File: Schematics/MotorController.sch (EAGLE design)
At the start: 47 parts, among them IC1 MEGA164P/324P/644P-AU, IC3 LM324N

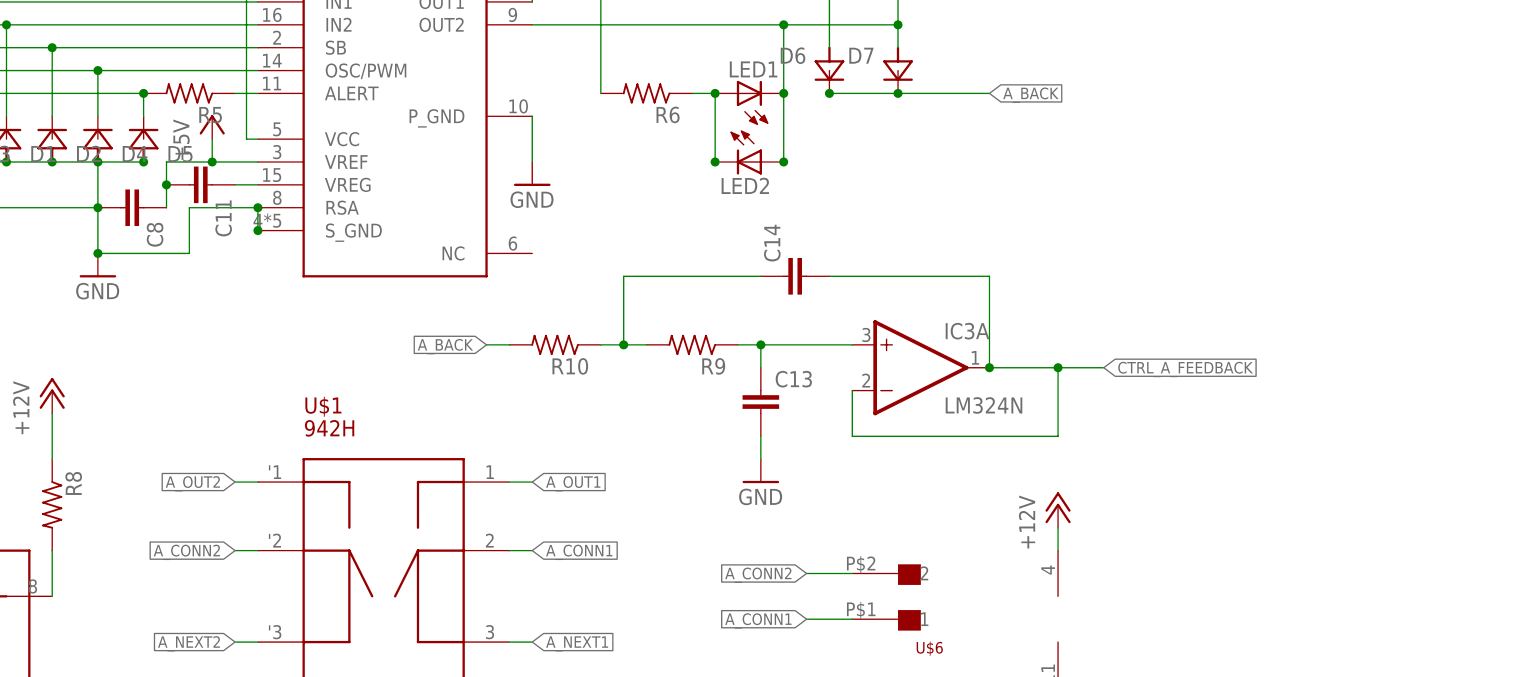
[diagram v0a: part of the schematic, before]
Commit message: add files of device software newly created
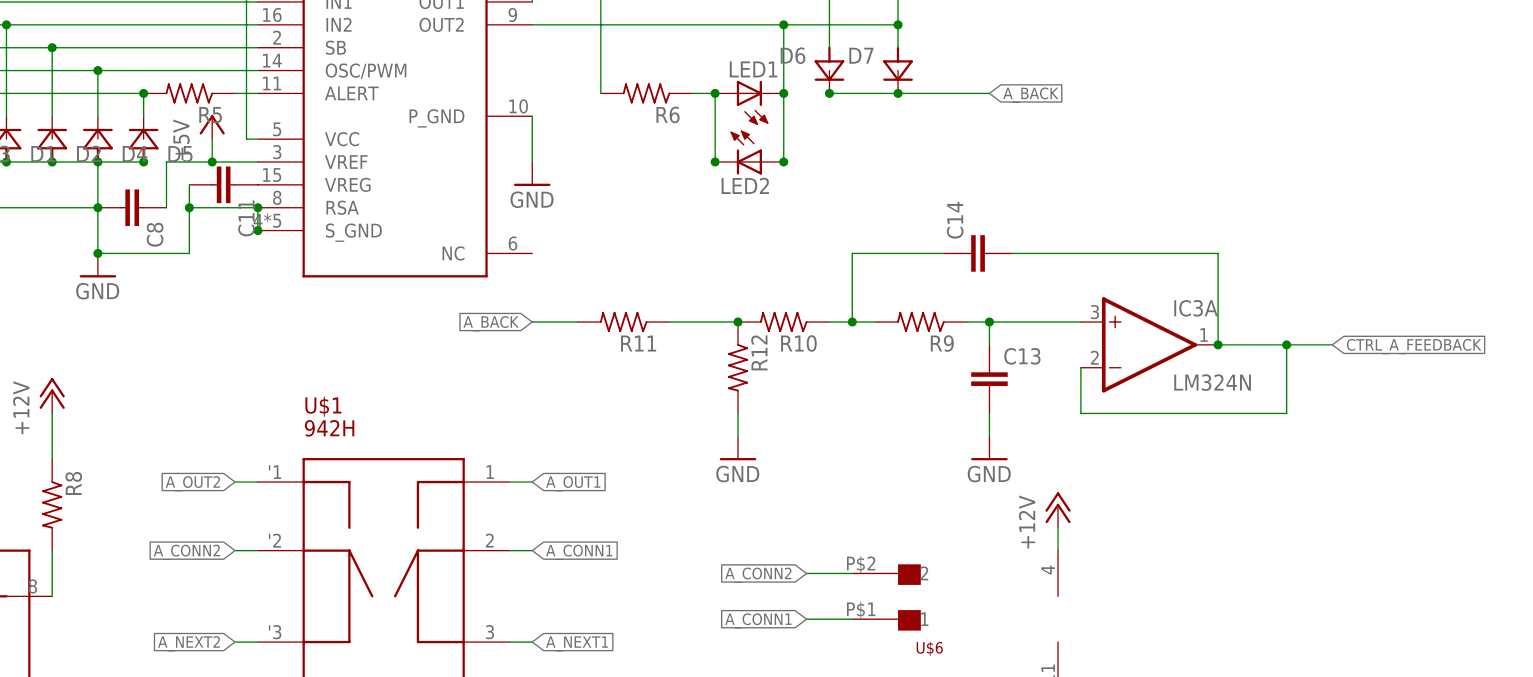
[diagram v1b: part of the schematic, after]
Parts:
- added R11, R12: (no value), rcl:R-US_M3216
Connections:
- new net N$14: R10.2, R11.1, R12.1
- net +5V: no longer C11.2
- net A_BACK: now also R11.2; no longer R10.2
- net GND: now also C11.2, R12.2
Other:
- moved on the sheet: C11, C13, C14, IC3A, R10, R9
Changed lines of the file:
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@@
 <part name="P+9" library="supply1" deviceset="+12V" device=""/>
 <part name="GND11" library="supply1" deviceset="GND" device=""/>
+<part name="R11" library="rcl" deviceset="R-US_" device="M3216"/>
+<part name="R12" library="rcl" deviceset="R-US_" device="M3216"/>
+<part name="GND12" library="supply1" deviceset="GND" device=""/>
 </parts>
 <sheets>
@@
 <instance part="C10" gate="G$1" x="226.06" y="154.94"/>
 <instance part="GND6" gate="1" x="226.06" y="142.24"/>
-<instance part="C11" gate="G$1" x="177.8" y="116.84" rot="R270"/>
+<instance part="C11" gate="G$1" x="180.34" y="116.84" rot="R270"/>
 <instance part="U$4" gate="G$1" x="185.42" y="157.48"/>
 <instance part="R4" gate="G$1" x="142.24" y="119.38" rot="R90"/>
@@
 <instance part="C12" gate="G$1" x="119.38" y="124.46"/>
 <instance part="GND7" gate="1" x="213.36" y="116.84"/>
-<instance part="IC3" gate="A" x="256.54" y="96.52"/>
+<instance part="IC3" gate="A" x="281.94" y="99.06"/>
 <instance part="LED1" gate="G$1" x="236.22" y="127" rot="R90"/>
 <instance part="LED2" gate="G$1" x="238.76" y="119.38" rot="R270"/>
@@
 <instance part="U$6" gate="G$1" x="254" y="76.2" rot="R180"/>
 <instance part="U$7" gate="G$1" x="254" y="58.42" rot="R180"/>
-<instance part="R9" gate="G$1" x="231.14" y="99.06" rot="R180"/>
-<instance part="R10" gate="G$1" x="215.9" y="99.06" rot="R180"/>
-<instance part="C13" gate="G$1" x="238.76" y="93.98"/>
-<instance part="C14" gate="G$1" x="241.3" y="106.68" rot="R90"/>
-<instance part="GND10" gate="1" x="238.76" y="83.82"/>
+<instance part="R9" gate="G$1" x="256.54" y="101.6" rot="R180"/>
+<instance part="R10" gate="G$1" x="241.3" y="101.6" rot="R180"/>
+<instance part="C13" gate="G$1" x="264.16" y="96.52"/>
+<instance part="C14" gate="G$1" x="261.62" y="109.22" rot="R90"/>
+<instance part="GND10" gate="1" x="264.16" y="86.36"/>
 <instance part="L2" gate="G$1" x="12.7" y="83.82" rot="R90"/>
 <instance part="IC3" gate="P" x="271.78" y="68.58"/>
 <instance part="P+9" gate="1" x="271.78" y="81.28"/>
 <instance part="GND11" gate="1" x="271.78" y="55.88"/>
+<instance part="R11" gate="G$1" x="223.52" y="101.6" rot="R180"/>
+<instance part="R12" gate="G$1" x="236.22" y="96.52" rot="R270"/>
+<instance part="GND12" gate="1" x="236.22" y="86.36"/>
 </instances>
 <busses>
@@
 </segment>
 <segment>
-<pinref part="C8" gate="G$1" pin="1"/>
-<wire x1="172.72" y1="114.3" x2="172.72" y2="116.84" width="0.1524" layer="91"/>
-<wire x1="172.72" y1="116.84" x2="172.72" y2="119.38" width="0.1524" layer="91"/>
 <wire x1="182.88" y1="119.38" x2="177.8" y2="119.38" width="0.1524" layer="91"/>
 <pinref part="P+3" gate="1" pin="+5V"/>
@@
 <wire x1="177.8" y1="121.92" x2="177.8" y2="119.38" width="0.1524" layer="91"/>
 <junction x="177.8" y="119.38"/>
-<pinref part="C11" gate="G$1" pin="2"/>
-<junction x="172.72" y="116.84"/>
 <pinref part="U$3" gate="G$1" pin="VREF"/>
+<pinref part="C8" gate="G$1" pin="1"/>
+<wire x1="172.72" y1="119.38" x2="172.72" y2="114.3" width="0.1524" layer="91"/>
 </segment>
 </net>
@@
 <junction x="170.18" y="119.38"/>
 <junction x="182.88" y="114.3"/>
+<pinref part="C11" gate="G$1" pin="2"/>
+<wire x1="175.26" y1="116.84" x2="175.26" y2="114.3" width="0.1524" layer="91"/>
+<junction x="175.26" y="114.3"/>
 </segment>
 <segment>
@@
 <pinref part="C13" gate="G$1" pin="2"/>
 <pinref part="GND10" gate="1" pin="GND"/>
-<wire x1="238.76" y1="88.9" x2="238.76" y2="86.36" width="0.1524" layer="91"/>
+<wire x1="264.16" y1="91.44" x2="264.16" y2="88.9" width="0.1524" layer="91"/>
 </segment>
 <segment>
@@
 <pinref part="GND11" gate="1" pin="GND"/>
 <wire x1="271.78" y1="58.42" x2="271.78" y2="60.96" width="0.1524" layer="91"/>
+</segment>
+<segment>
+<pinref part="R12" gate="G$1" pin="2"/>
+<pinref part="GND12" gate="1" pin="GND"/>
+<wire x1="236.22" y1="91.44" x2="236.22" y2="88.9" width="0.1524" layer="91"/>
 </segment>
 </net>
@@
 <segment>
 <pinref part="C11" gate="G$1" pin="1"/>
-<wire x1="180.34" y1="116.84" x2="182.88" y2="116.84" width="0.1524" layer="91"/>
 <pinref part="U$3" gate="G$1" pin="VREG"/>
 </segment>
@@
 <segment>
 <pinref part="C14" gate="G$1" pin="2"/>
-<wire x1="246.38" y1="106.68" x2="264.16" y2="106.68" width="0.1524" layer="91"/>
+<wire x1="266.7" y1="109.22" x2="289.56" y2="109.22" width="0.1524" layer="91"/>
 <pinref part="IC3" gate="A" pin="OUT"/>
-<wire x1="264.16" y1="106.68" x2="264.16" y2="96.52" width="0.1524" layer="91"/>
-<wire x1="264.16" y1="96.52" x2="271.78" y2="96.52" width="0.1524" layer="91"/>
+<wire x1="289.56" y1="109.22" x2="289.56" y2="99.06" width="0.1524" layer="91"/>
+<wire x1="289.56" y1="99.06" x2="297.18" y2="99.06" width="0.1524" layer="91"/>
 <pinref part="IC3" gate="A" pin="-IN"/>
-<wire x1="248.92" y1="93.98" x2="248.92" y2="88.9" width="0.1524" layer="91"/>
-<wire x1="248.92" y1="88.9" x2="271.78" y2="88.9" width="0.1524" layer="91"/>
-<wire x1="271.78" y1="88.9" x2="271.78" y2="96.52" width="0.1524" layer="91"/>
-<wire x1="271.78" y1="96.52" x2="276.86" y2="96.52" width="0.1524" layer="91"/>
-<junction x="264.16" y="96.52"/>
-<junction x="271.78" y="96.52"/>
-<label x="276.86" y="96.52" size="1.27" layer="95" xref="yes"/>
+<wire x1="274.32" y1="96.52" x2="274.32" y2="91.44" width="0.1524" layer="91"/>
+<wire x1="274.32" y1="91.44" x2="297.18" y2="91.44" width="0.1524" layer="91"/>
+<wire x1="297.18" y1="91.44" x2="297.18" y2="99.06" width="0.1524" layer="91"/>
+<wire x1="297.18" y1="99.06" x2="302.26" y2="99.06" width="0.1524" layer="91"/>
+<junction x="289.56" y="99.06"/>
+<junction x="297.18" y="99.06"/>
+<label x="302.26" y="99.06" size="1.27" layer="95" xref="yes"/>
 </segment>
 </net>
@@
 </segment>
 <segment>
-<pinref part="R10" gate="G$1" pin="2"/>
-<wire x1="210.82" y1="99.06" x2="208.28" y2="99.06" width="0.1524" layer="91"/>
-<label x="208.28" y="99.06" size="1.27" layer="95" rot="R180" xref="yes"/>
+<pinref part="R11" gate="G$1" pin="2"/>
+<wire x1="218.44" y1="101.6" x2="213.36" y2="101.6" width="0.1524" layer="91"/>
+<label x="213.36" y="101.6" size="1.27" layer="95" rot="R180" xref="yes"/>
 </segment>
 </net>
@@
 <pinref part="R10" gate="G$1" pin="1"/>
 <pinref part="R9" gate="G$1" pin="2"/>
-<wire x1="220.98" y1="99.06" x2="223.52" y2="99.06" width="0.1524" layer="91"/>
-<wire x1="223.52" y1="99.06" x2="226.06" y2="99.06" width="0.1524" layer="91"/>
-<wire x1="223.52" y1="99.06" x2="223.52" y2="106.68" width="0.1524" layer="91"/>
+<wire x1="246.38" y1="101.6" x2="248.92" y2="101.6" width="0.1524" layer="91"/>
+<wire x1="248.92" y1="101.6" x2="251.46" y2="101.6" width="0.1524" layer="91"/>
+<wire x1="248.92" y1="101.6" x2="248.92" y2="109.22" width="0.1524" layer="91"/>
 <pinref part="C14" gate="G$1" pin="1"/>
-<wire x1="223.52" y1="106.68" x2="238.76" y2="106.68" width="0.1524" layer="91"/>
-<junction x="223.52" y="99.06"/>
+<wire x1="248.92" y1="109.22" x2="259.08" y2="109.22" width="0.1524" layer="91"/>
+<junction x="248.92" y="101.6"/>
 </segment>
 </net>
@@
 <pinref part="R9" gate="G$1" pin="1"/>
 <pinref part="IC3" gate="A" pin="+IN"/>
-<wire x1="236.22" y1="99.06" x2="238.76" y2="99.06" width="0.1524" layer="91"/>
+<wire x1="261.62" y1="101.6" x2="264.16" y2="101.6" width="0.1524" layer="91"/>
 <pinref part="C13" gate="G$1" pin="1"/>
-<wire x1="238.76" y1="99.06" x2="248.92" y2="99.06" width="0.1524" layer="91"/>
-<wire x1="238.76" y1="99.06" x2="238.76" y2="96.52" width="0.1524" layer="91"/>
-<junction x="238.76" y="99.06"/>
+<wire x1="264.16" y1="101.6" x2="274.32" y2="101.6" width="0.1524" layer="91"/>
+<wire x1="264.16" y1="101.6" x2="264.16" y2="99.06" width="0.1524" layer="91"/>
+<junction x="264.16" y="101.6"/>
 </segment>
 </net>
@@
 </segment>
 </net>
+<net name="N$14" class="0">
+<segment>
+<pinref part="R10" gate="G$1" pin="2"/>
+<pinref part="R12" gate="G$1" pin="1"/>
+<pinref part="R11" gate="G$1" pin="1"/>
+<wire x1="236.22" y1="101.6" x2="228.6" y2="101.6" width="0.1524" layer="91"/>
+<junction x="236.22" y="101.6"/>
+</segment>
+</net>

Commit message: restoring
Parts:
- removed D5, D6, D7, D8: 1SS196, myparts:1SS196
- removed L2: (no value), rcl:L-USL3216C
- removed U$5: TLP621-2, myparts:TLP621-2
- removed U$6, U$7: XH-2, myparts:XH-2
- added A, B, C, D: 942H, myparts:942H
- added A_NEXT, A_PREV, B_NEXT, B_PREV, C_NEXT, C_PREV, D_NEXT, D_PREV: XH-2, myparts:XH-2
- added C15, C18, C19, C24, C25: 0.1u, rcl:C-EUC0603
- added C16, C17: 0.47u, rcl:C-EUC0603
- added C20, C21: 22p, rcl:C-EUC0603
- added C22, C23: 4.7u, rcl:C-EUC0603
- added C26, C27: (no value), rcl:CPOL-EUE2,5-6E
- added CONN: TUS_MODULE_SUPPLY, tus:TUS_MODULE_SUPPLY
- added F1, F2, F3, F4, F5: POLYSWITCH_20204/5, myparts:POLYSWITCH_20204/5
- added IC2: MEGA164P/324P/644P-AU, avr-7:MEGA164P/324P/644P-AU
- added IC4: TLP621-2, myparts:TLP621-2
- added LED3, LED5, LED7: G, led:LED3MM
- added LED4, LED6, LED8: O, led:LED3MM
- added R13, R14, R23, R24: 100, resistor:R-EU_R0603
- added R15, R16, R22, R25: 25k, resistor:R-EU_R0603
- added R17, R18, R20, R21, R30, R31: 3.3k, resistor:R-EU_R0603
- added R19, R36, R37: 10k, resistor:R-EU_R0603
- added R26, R27: 0.01, resistor:R-EU_R1206
- added R28, R29: 33k, resistor:R-EU_R0603
- added R32, R33: 500, resistor:R-EU_R0603
- added R34, R35: 100k, resistor:R-EU_R0603
- added T1, T2, T3, T4: 2SC1815, myparts:2SC1815
- C1, C2: device rcl:C-EUC1608 -> rcl:CPOL-EUE2,5-6E
- C10: value (none) -> 0.47u; device rcl:CPOL-EUE2-5 -> rcl:C-EUC0603
- C11, C7, C8: value (none) -> 0.1u; device rcl:C-EUC1608 -> rcl:C-EUC0603
- C12: value (none) -> 100u; device rcl:C-EUC1608 -> rcl:CPOL-EUE2.5-6
- C13: value (none) -> 0.1u; device rcl:C-EUC3216 -> rcl:C-EUC0603
- C14: value (none) -> 100u; device rcl:C-EUC3216 -> rcl:CPOL-EUE2-5
- C3: value (none) -> 0.1u; device rcl:CPOL-EUE2-5 -> rcl:C-EUC0603
- C4: value (none) -> 0.1u; device rcl:CPOL-EUE2.5-6 -> rcl:C-EUC0603
- C5, C6: value (none) -> 4.7u; device rcl:C-EUC1608 -> rcl:C-EUC0603
- C9: value (none) -> 0.47u; device rcl:C-EUC1608 -> rcl:C-EUC0603
- D1, D2, D3, D4: value 1SS196 -> 1N4148DO35-7; device myparts:1SS196 -> diode:1N4148DO35-7
- IC1: value MEGA164P/324P/644P-AU -> TLP621-2; device avr-7:MEGA164P/324P/644P-AU -> myparts:TLP621-2
- IC3: value LM324N -> OPA4234P; device linear:LM324N -> burr-brown:OPA4234P
- JP1: value AVR-JTAG-10-R -> AVR-JTAG-10; device avr-7:AVR-JTAG-10-R -> avr-7:AVR-JTAG-10
- L1: value (none) -> 47u; device rcl:L-USL3216C -> rcl:L-EUL3216C
- LED1: value (none) -> G
- LED2: value (none) -> O
- Q1: value (none) -> 20.000M
- R1, R6: value (none) -> 100k; device rcl:R-US_M3216 -> resistor:R-EU_R0603
- R10, R9: value (none) -> 33k; device rcl:R-US_M3216 -> resistor:R-EU_R0603
- R11, R12: value (none) -> 0.01; device rcl:R-US_M3216 -> resistor:R-EU_R1206
- R2, R4: value 100k -> 10k; device rcl:R-US_M3216 -> resistor:R-EU_R0603
- R3: value 100k -> 500; device rcl:R-US_M3216 -> resistor:R-EU_R0603
- R5: value (none) -> 500; device rcl:R-US_M3216 -> resistor:R-EU_R0603
- R7, R8: value (none) -> 3.3k; device rcl:R-US_M3216 -> resistor:R-EU_R0603
- U$1: value 942H -> TB6559; device myparts:942H -> myparts:TB6559
- U$2: value TUS_MODULE_SUPPLY -> TB6559; device tus:TUS_MODULE_SUPPLY -> myparts:TB6559
- U$4: value POLYSWITCH_20207/10 -> TB6559; device myparts:POLYSWITCH_20207/10 -> myparts:TB6559
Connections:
- removed net A_BACK: D6.A, D7.A, R11.2
- removed net A_CONN1: U$1.2, U$6.1
- removed net A_CONN2: U$1.'2, U$6.2
- removed net A_NEXT1: U$1.3, U$7.1
- removed net A_NEXT2: U$1.'3, U$7.2
- removed net CTRL_A_FEEDBACK: C14.2, IC1.(ADC0/PCINT0)PA0, IC3A.-IN, IC3A.OUT
- removed net CTRL_B_FEEDBACK: IC1.(ADC1/PCINT1)PA1
- removed net CTRL_C_FEEDBACK: IC1.(ADC2/PCINT2)PA2
- removed net CTRL_D_FEEDBACK: IC1.(ADC3/PCINT3)PA3
- removed net CTRL_PWM: D4.A, U$3.OSC/PWM
- new net A_OUT3: C.1, R20.2, U$3.OUT1
- new net A_OUT4: C.'1, LED5.A, LED6.C, U$3.OUT2
- new net A_OUT5: B.1, R18.2, U$2.OUT1
- new net A_OUT6: B.'1, LED1.A, LED2.C, U$2.OUT2
- new net A_OUT7: D.1, R21.2, U$4.OUT1
- new net A_OUT8: D.'1, LED7.A, LED8.C, U$4.OUT2
- new net D: D.3, D_PREV.2
- new net FEEDBACK_A: IC2.(ADC2/PCINT2)PA2, IC3A.OUT, R16.2
- new net FEEDBACK_B: IC2.(ADC3/PCINT3)PA3, IC3B.OUT, R15.2
- new net FEEDBACK_C: IC2.(ADC1/PCINT1)PA1, IC3D.OUT, R25.2
- new net FEEDBACK_D: IC2.(ADC0/PCINT0)PA0, IC3C.OUT, R22.2
- new net N$15: A.'2, A_NEXT.1
- new net N$16: A.3, A_PREV.2
- new net N$17: A.'3, A_PREV.1
- new net N$18: C18.2, C27.+, F4.1, U$3.VCC
- new net N$19: LED5.C, LED6.A, R20.1
- new net N$20: IC1G$2.1, R5.2
- new net N$21: C9.1, IC3A.+IN, R9.2
- new net N$22: C.2, C_NEXT.2
- new net N$23: C.'2, C_NEXT.1
- new net N$24: C.3, C_PREV.2
- new net N$25: C.'3, C_PREV.1
- new net N$26: IC4G$2.4, R35.1, R36.1
- new net N$27: C.'4, D3.C, T3.E
- new net N$28: R36.2, T3.B
- new net N$29: IC3D.-IN, R24.1, R25.1
- new net N$30: C16.1, IC3D.+IN, R28.2
- new net N$31: R26.1, R28.1, U$3.P_GND
- new net N$32: C4.1, U$2.VREG
- new net N$33: R8.1, U$2.ALERT
- new net N$34: C2.+, C8.2, F1.1, U$2.VCC
- new net N$35: LED1.C, LED2.A, R18.1
- new net N$36: IC4G$1.1, R33.2
- new net N$37: B.2, B_NEXT.2
- new net N$38: B.'2, B_NEXT.1
- new net N$39: B.3, B_PREV.2
- new net N$40: B.'3, B_PREV.1
- new net N$41: IC1G$2.4, R1.1, R4.1
- new net N$42: B.'4, D2.C, T1.E
- new net N$43: R4.2, T1.B
- new net N$44: IC3B.-IN, R13.1, R15.1
- new net N$45: C10.1, IC3B.+IN, R10.2
- new net N$46: R10.1, R12.1, U$2.P_GND
- new net N$47: C25.1, U$4.VREG
- new net N$48: R31.1, U$4.ALERT
- new net N$49: C19.2, C26.+, F5.1, U$4.VCC
- new net N$50: LED7.C, LED8.A, R21.1
- new net N$51: IC4G$2.1, R32.2
- new net N$52: D.2, D_NEXT.2
- new net N$53: D.'2, D_NEXT.1
- new net N$54: CONN.6_5V, F3.1
- new net N$55: D.'3, D_PREV.1
- new net N$56: IC4G$1.4, R34.1, R37.1
- new net N$57: D.'4, D4.C, T4.E
- new net N$58: R37.2, T4.B
- new net N$59: IC3C.-IN, R22.1, R23.1
- new net N$60: C17.1, IC3C.+IN, R29.2
- new net N$61: R27.1, R29.1, U$4.P_GND
- new net N$84: A.'4, D1.C, T2.E
- new net N$86: R2.2, T2.B
- net !RESET: now also CONN.15_!RESET, IC2.!RESET, JP1.6, R19.2; no longer IC1.!RESET, R1.2, U$2.15_!RESET
- net !SS: now also CONN.11_!SS, IC2.(OC0B/!SS!/PCINT12)PB4; no longer IC1.(OC0B/!SS!/PCINT12)PB4, U$2.11_!SS
- net +12V: now also C12.+, CONN.1_12V, CONN.2_12V, CONN.4_12V, F1.2, F2.2, F4.2, F5.2, IC1G$1.3, IC1G$2.3, IC4G$1.3, IC4G$2.3, T1.C, T2.C, T3.C, T4.C; no longer C10.+, C4.+, C9.2, D8.A, IC3P.V+, R8.1, U$2.1_12V, U$2.2_12V, U$2.4_12V, U$4.2
- net +5V: now also C11.2, C13.2, C14.+, C15.2, F3.2, IC2.VCC@1, IC2.VCC@2, IC2.VCC@3, IC3A.V+, R19.1, U$1.VREF, U$2.VREF, U$4.VREF; no longer C3.+, C5.2, C6.2, C7.2, C8.1, IC1.VCC@1, IC1.VCC@2, IC1.VCC@3, L2.1, R1.1, U$2.6_5V
- net A_OUT1: now also A.1, R17.2, U$1.OUT1; no longer D6.C, R6.2, U$1.1, U$3.OUT1
- net A_OUT2: now also A.'1, LED3.A, LED4.C, U$1.OUT2; no longer D7.C, LED1.C, LED2.A, U$1.'1, U$3.OUT2
- net CTRL_A_1: now also IC2.(ADC5/PCINT5)PA5, U$1.IN1; no longer D3.A, IC1.(RXD0/PCINT24)PD0, R2.2, U$3.IN1
- net CTRL_A_2: now also IC2.(ADC6/PCINT6)PA6, U$1.IN2; no longer D1.A, IC1.(TXD0/PCINT25)PD1, R3.2, U$3.IN2
- net CTRL_A_3: now also IC2.(ADC4/PCINT4)PA4, R3.1, U$1.SB; no longer D2.A, IC1.(RXD1/INT0/PCINT26)PD2, R4.2, R7.1, U$3.SB
- net CTRL_A_ALERT: now also C5.1, IC2.(ADC7/PCINT7)PA7, R7.2; no longer C12.1, D5.A, IC1.(TXD1/INT1/PCINT27)PD3, R5.2
- net CTRL_A_PWM: now also IC2.(OC2B/ICP/PCINT30)PD6, U$1.OSC/PWM; no longer IC1.(OC1A/PCINT29)PD5
- net CTRL_B_1: now also IC2.(INT2/AIN0/PCINT10)PB2, U$2.IN1; no longer IC1.(SCL/PCINT16)PC0
- net CTRL_B_2: now also IC2.(CLKO/T1/PCINT9)PB1, U$2.IN2; no longer IC1.(SDA/PCINT17)PC1
- net CTRL_B_3: now also IC2.(OC0A/AIN1/PCINT11)PB3, R5.1, U$2.SB; no longer IC1.(TOSC1/PCINT22)PC6
- net CTRL_B_ALERT: now also C6.1, IC2.(XCK0/T0/PCINT8)PB0, R8.2; no longer IC1.(TOSC2/PCINT23)PC7
- net CTRL_B_PWM: now also IC2.(XCK1/OC1B/PCINT28)PD4, U$2.OSC/PWM; no longer IC1.(XCK1/OC1B/PCINT28)PD4
- net CTRL_C_1: now also IC2.(RXD1/INT0/PCINT26)PD2, U$3.IN1; no longer IC1.(XCK0/T0/PCINT8)PB0
- net CTRL_C_2: now also IC2.(TXD0/PCINT25)PD1, U$3.IN2; no longer IC1.(CLKO/T1/PCINT9)PB1
- net CTRL_C_3: now also IC2.(TXD1/INT1/PCINT27)PD3, R32.1, U$3.SB; no longer IC1.(INT2/AIN0/PCINT10)PB2
- net CTRL_C_ALERT: now also C22.1, IC2.(RXD0/PCINT24)PD0, R30.2; no longer IC1.(OC0A/AIN1/PCINT11)PB3
- net CTRL_C_PWM: now also IC2.(OC2A/PCINT31)PD7, U$3.OSC/PWM; no longer IC1.(OC2A/PCINT31)PD7
- net CTRL_D_1: now also IC2.(TOSC2/PCINT23)PC7, U$4.IN1; no longer IC1.(ADC4/PCINT4)PA4
- net CTRL_D_2: now also IC2.(TOSC1/PCINT22)PC6, U$4.IN2; no longer IC1.(ADC5/PCINT5)PA5
- net CTRL_D_3: now also IC2.(SCL/PCINT16)PC0, R33.1, U$4.SB; no longer IC1.(ADC6/PCINT6)PA6
- net CTRL_D_ALERT: now also C23.1, IC2.(SDA/PCINT17)PC1, R31.2; no longer IC1.(ADC7/PCINT7)PA7
- net CTRL_D_PWM: now also IC2.(OC1A/PCINT29)PD5, U$4.OSC/PWM; no longer IC1.(OC2B/ICP/PCINT30)PD6
- net GND: now also A.4, B.4, C.4, C1.-, C10.2, C11.1, C12.-, C13.1, C14.-, C15.1, C16.2, C17.2, C18.1, C19.1, C2.-, C20.1, C21.1, C22.2, C23.2, C24.2, C25.2, C26.-, C27.-, C3.2, C4.2, C5.2, C6.2, C8.1, C9.2, CONN.12_GND, CONN.3_GND, CONN.5_GND, CONN.7_GND, CONN.8_GND, CONN.9_GND, D.4, D1.A, D2.A, D3.A, D4.A, IC1G$1.2, IC1G$2.2, IC2.GND@1, IC2.GND@2, IC2.GND@3, IC2.GND@4, IC3A.V-, IC4G$1.2, IC4G$2.2, R1.2, R11.2, R13.2, R14.2, R23.2, R24.2, R26.2, R27.2, R34.2, R35.2, R6.2, U$1.RSA, U$1.S_GND, U$2.RSA, U$2.S_GND, U$4.RSA, U$4.S_GND; no longer C1.1, C10.-, C11.2, C12.2, C13.2, C2.1, C3.-, C4.-, C5.1, C6.1, C8.2, C9.1, D1.C, D2.C, D3.C, D4.C, D5.C, D8.C, IC1.GND@1, IC1.GND@2, IC1.GND@3, IC1.GND@4, IC3P.V-, R2.1, R3.1, R4.1, U$1.4, U$2.12_GND, U$2.3_GND, U$2.5_GND, U$2.7_GND, U$2.8_GND, U$2.9_GND, U$3.P_GND, U$5G$1.2
- net MISO: now also CONN.14_MISO, IC2.(MISO/PCINT14)PB6; no longer IC1.(MISO/PCINT14)PB6, U$2.14_MISO
- net MOSI: now also CONN.16_MOSI, IC2.(MOSI/PCINT13)PB5; no longer IC1.(MOSI/PCINT13)PB5, U$2.16_MOSI
- net N$1: now also IC2.AREF, IC2.AVCC; no longer IC1.AVCC
- net N$10: now also C1.+, C7.2, F2.1, U$1.VCC; no longer U$3.VCC, U$4.1
- net N$11: now also IC3A.-IN, R14.1, R16.1; no longer C14.1, R10.1, R9.2
- net N$12: now also R30.1, U$3.ALERT; no longer C13.1, IC3A.+IN, R9.1
- net N$13: now also A.2, A_NEXT.2; no longer IC1.AREF, L2.2
- net N$14: now also R9.1, U$1.P_GND; no longer R10.2, R12.1
- net N$2: now also C21.2, IC2.XTAL2; no longer C1.2, IC1.XTAL2
- net N$3: now also C20.2, IC2.XTAL1; no longer C2.2, IC1.XTAL1
- net N$4: now also R7.1, U$1.ALERT; no longer R5.1, U$3.ALERT
- net N$5: now also C3.1, U$1.VREG; no longer C11.1, U$3.VREG
- net N$6: now also IC1G$1.1, R3.2; no longer R7.2, U$5G$1.1
- net N$7: now also IC1G$1.4, R2.1, R6.1; no longer U$1.'4, U$5G$1.4
- net N$8: now also LED3.C, LED4.A, R17.1; no longer LED1.A, LED2.C, R6.1
- net N$9: now also C24.1, U$3.VREG; no longer R8.2, U$5G$1.3
- net SCK: now also CONN.13_SCK, IC2.(SCK/PCINT15)PB7; no longer IC1.(SCK/PCINT15)PB7, U$2.13_SCK
- net TCK: now also IC2.(TCK/PCINT18)PC2; no longer IC1.(TCK/PCINT18)PC2
- net TDI: now also IC2.(TDI/PCINT21)PC5; no longer IC1.(TDI/PCINT21)PC5
- net TDO: now also IC2.(TDO/PCINT20)PC4; no longer IC1.(TDO/PCINT20)PC4
- net TMS: now also IC2.(TMS/PCINT19)PC3; no longer IC1.(TMS/PCINT19)PC3
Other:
- moved on the sheet: C11, C13, C5, C6, C7, C8, C9, D1, D2, D3, D4, JP1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
